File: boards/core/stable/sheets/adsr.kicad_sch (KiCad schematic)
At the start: 28 parts, among them U212 4002, U213 LM358, U214 TL072, U215 CD4053B

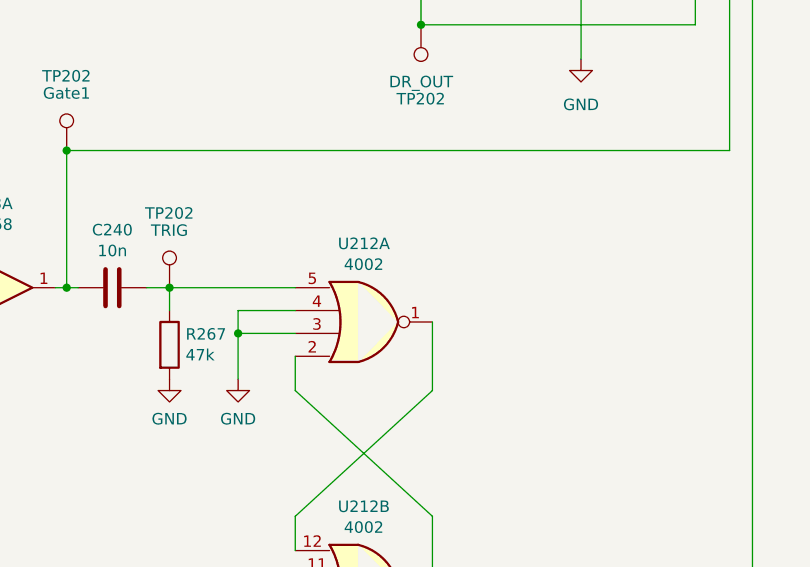
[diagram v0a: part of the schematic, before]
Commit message: Updated and checked Core board BOM
ref https://github.com/shmoergh/hog/issues/19
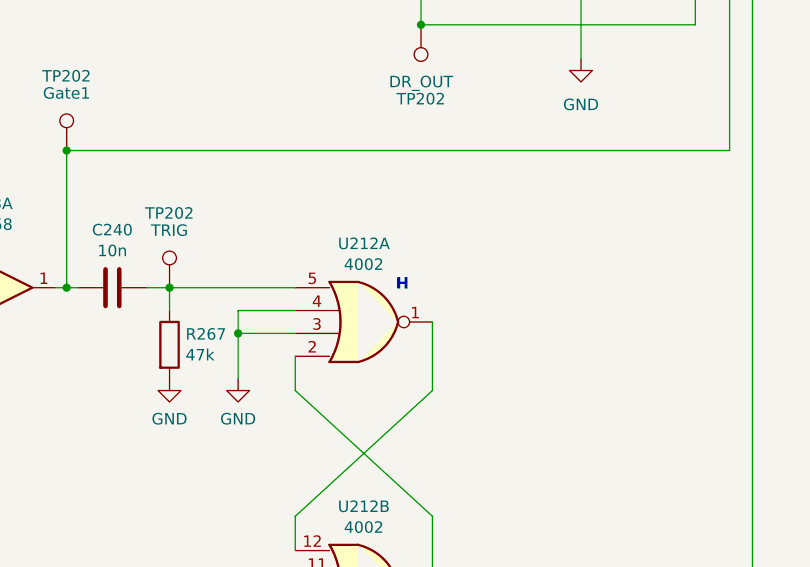
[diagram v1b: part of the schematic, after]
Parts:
- C203, C240, D202, R206, R265, R266, R267, R269, U213, U214, U215: Vendor (none) -> JLCPCB
- C241: Part No. (none) -> 598-106RSS050M; Part URL (none) -> https://mou.sr/3VxA0hV; Vendor (none) -> Mouser; now in the parts list
- R268: Part No. (none) -> 303-CFR0W4J0471B00; Part URL (none) -> https://mou.sr/49DiyPd; Vendor (none) -> Mouser; now in the parts list
- RV_ADSR_MAX_VOLTAGE201: Part No. (none) -> 652-3006P-1-104-LF; Part URL (none) -> https://mou.sr/4ff5W1E; Vendor (none) -> Mouser; now in the parts list
- U212: Part No. (none) -> 595-CD4002BE; Part URL (none) -> https://mou.sr/3JJTry1; Vendor (none) -> Mouser; now in the parts list

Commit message: Added Core Mouser BOM csv and Production readme
ref https://github.com/shmoergh/hog/issues/19
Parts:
- R268: Part No. 303-CFR0W4J0471B00 -> 603-CFR50SJT-52-470R; Part URL https://mou.sr/49DiyPd -> https://mou.sr/49C5zwV
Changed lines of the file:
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@@
 			)
 		)
-		(property "Part No." "303-CFR0W4J0471B00 "
+		(property "Part No." "603-CFR50SJT-52-470R "
 			(at 163.83 53.34 0)
 			(effects
@@
 			)
 		)
-		(property "Part URL" "https://mou.sr/49DiyPd"
+		(property "Part URL" "https://mou.sr/49C5zwV"
 			(at 163.83 53.34 0)
 			(effects

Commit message: Updated resistor Mouser no's and added full bom
- Some of the THT resistors in the BOM were referencing to products with min. 1000 pcs order quantity
- Added a full Mouser BOM which can be used to order all Mouser components by uploading to their BOM tool: https://hu.mouser.com/bom/
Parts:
- R268: Part No. 603-CFR50SJT-52-470R -> 603-MFR-25FBF52-470R; Part URL https://mou.sr/49C5zwV -> https://mou.sr/3FKKllB
